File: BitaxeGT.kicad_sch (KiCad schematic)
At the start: 11 parts

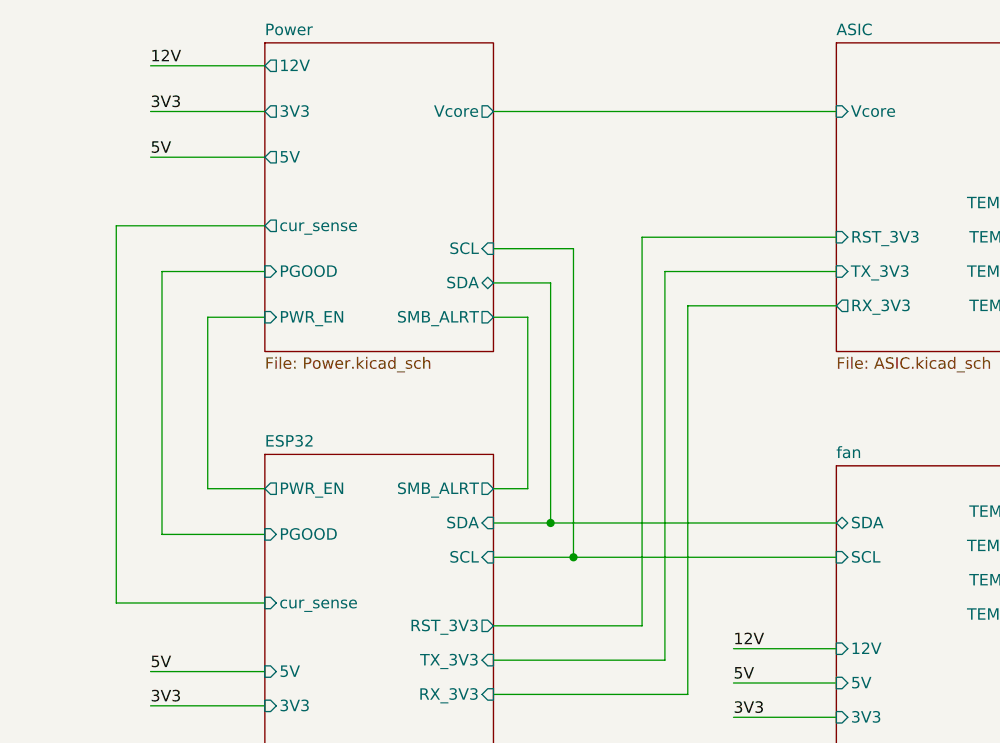
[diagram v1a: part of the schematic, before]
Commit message: fixed unused input on level shifter. Attached Vcore to ADC pin on the ESP32 for monitoring.
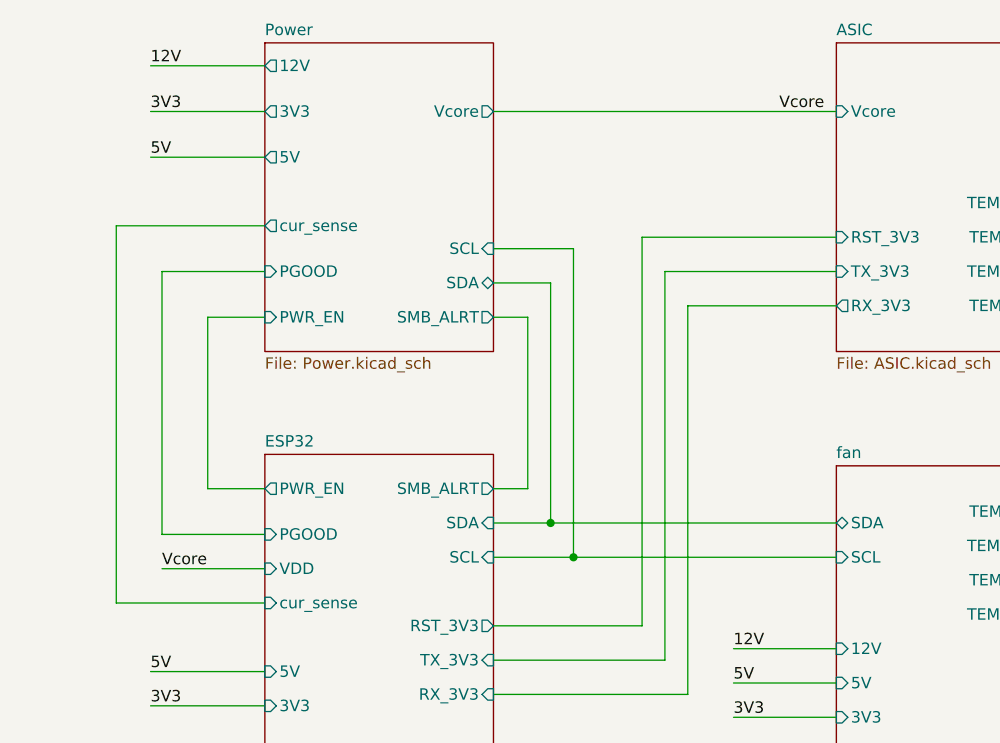
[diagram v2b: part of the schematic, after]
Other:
- sheet ESP32 ports: added VDD; removed none
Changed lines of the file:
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@@
+	(wire
+		(pts
+			(xy 105.41 101.6) (xy 116.84 101.6)
+		)
+		(stroke
+			(width 0)
+			(type default)
+		)
+	)
 	(wire
 		(pts
@@
 		)
 	)
-	(label "5V"
-		(at 104.14 55.88 0)
+	(label "Vcore"
+		(at 105.41 101.6 0)
 		(fields_autoplaced yes)
 		(effects
@@
 		)
 	)
-	(label "3V3"
-		(at 168.91 118.11 0)
+	(label "5V"
+		(at 104.14 55.88 0)
 		(fields_autoplaced yes)
 		(effects
@@
 		)
 	)
-	(label "5V"
-		(at 217.17 48.26 180)
+	(label "3V3"
+		(at 168.91 118.11 0)
 		(fields_autoplaced yes)
 		(effects
@@
 				(size 1.27 1.27)
 			)
-			(justify right bottom)
-		)
-	)
-	(label "3V3"
-		(at 217.17 52.07 180)
+			(justify left bottom)
+		)
+	)
+	(label "5V"
+		(at 217.17 48.26 180)
 		(fields_autoplaced yes)
 		(effects
@@
 		)
 	)
+	(label "3V3"
+		(at 217.17 52.07 180)
+		(fields_autoplaced yes)
+		(effects
+			(font
+				(size 1.27 1.27)
+			)
+			(justify right bottom)
+		)
+	)
 	(label "12V"
 		(at 104.14 45.72 0)
+		(fields_autoplaced yes)
+		(effects
+			(font
+				(size 1.27 1.27)
+			)
+			(justify left bottom)
+		)
+	)
+	(label "Vcore"
+		(at 173.99 50.8 0)
 		(fields_autoplaced yes)
 		(effects
@@
 			(effects
 				(font
+					(size 1.27 1.27)
+				)
+				(justify left)
+			)
+		)
+		(pin "VDD" input
+			(at 116.84 101.6 180)
+			(effects
+				(font

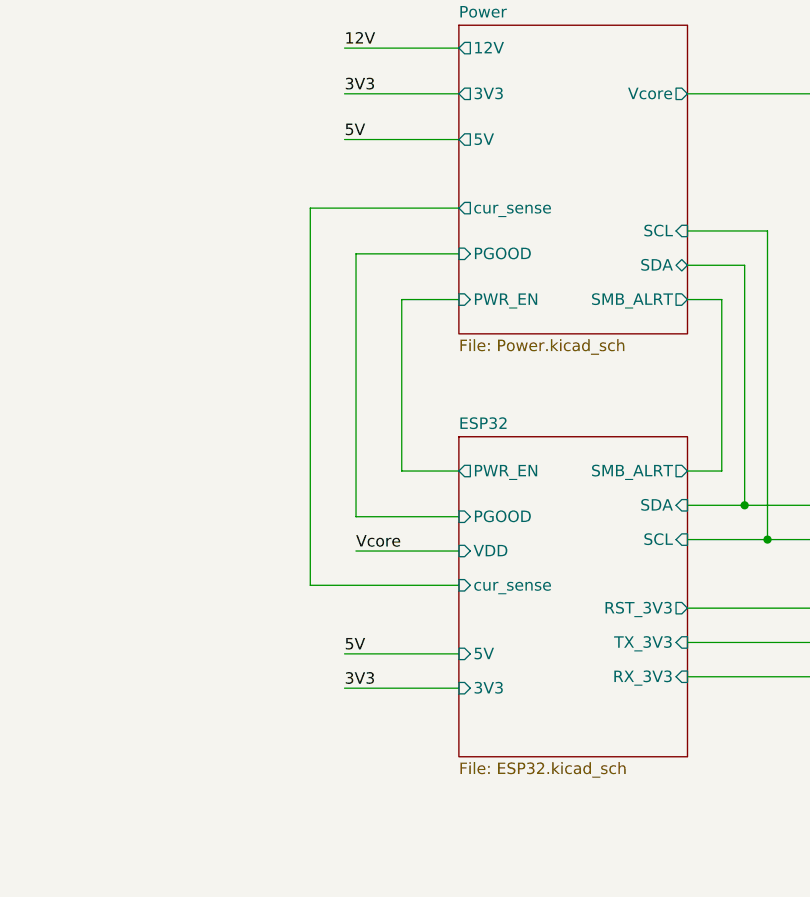
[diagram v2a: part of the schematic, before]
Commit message: added Vsupply to BAP. Cleaning up library paths. Moving 12V vias out of Bitaxe logo
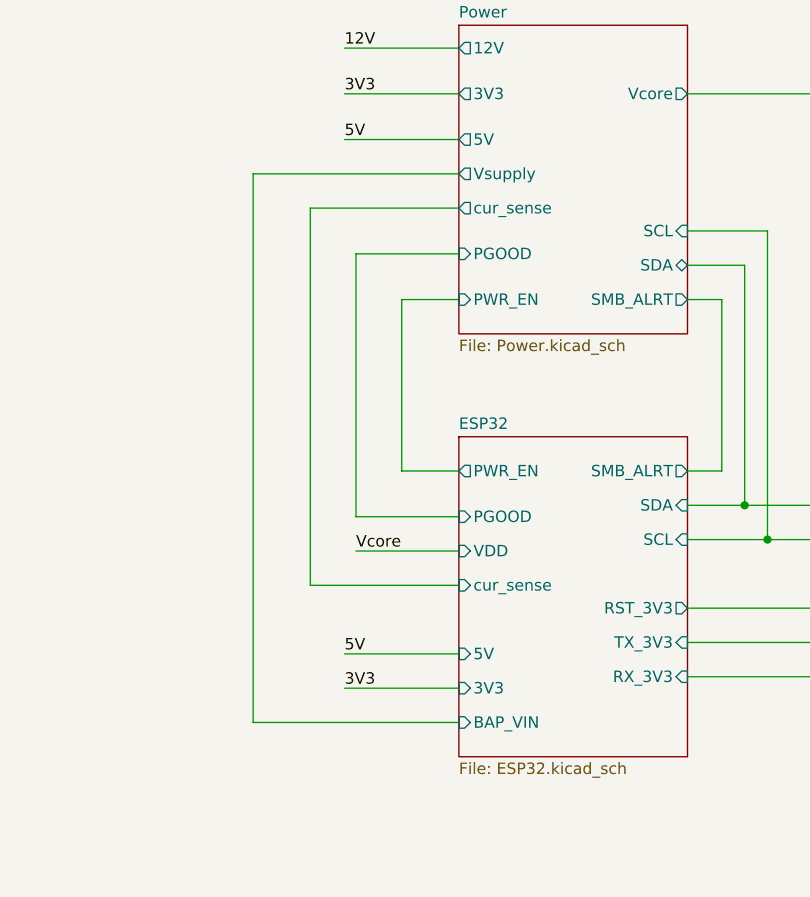
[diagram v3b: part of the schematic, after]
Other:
- sheet ESP32 ports: added BAP_VIN; removed none
- sheet Power ports: added Vsupply; removed none
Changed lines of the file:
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@@
+	(wire
+		(pts
+			(xy 116.84 59.69) (xy 93.98 59.69)
+		)
+		(stroke
+			(width 0)
+			(type default)
+		)
+	)
 	(wire
 		(pts
@@
 		(pts
 			(xy 104.14 113.03) (xy 116.84 113.03)
+		)
+		(stroke
+			(width 0)
+			(type default)
+		)
+	)
+	(wire
+		(pts
+			(xy 93.98 120.65) (xy 116.84 120.65)
+		)
+		(stroke
+			(width 0)
+			(type default)
+		)
+	)
+	(wire
+		(pts
+			(xy 93.98 59.69) (xy 93.98 120.65)
 		)
 		(stroke
@@
 			)
 		)
+		(pin "BAP_VIN" input
+			(at 116.84 120.65 180)
+			(effects
+				(font
+					(size 1.27 1.27)
+				)
+				(justify left)
+			)
+		)
 		(instances
 			(project "BitaxeGT"
@@
 			(effects
 				(font
+					(size 1.27 1.27)
+				)
+				(justify left)
+			)
+		)
+		(pin "Vsupply" output
+			(at 116.84 59.69 180)
+			(effects
+				(font

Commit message: BOM updates
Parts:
- HS1: now left out of the parts list
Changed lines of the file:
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@@
 		(unit 1)
 		(exclude_from_sim yes)
-		(in_bom yes)
+		(in_bom no)
 		(on_board yes)
 		(dnp no)

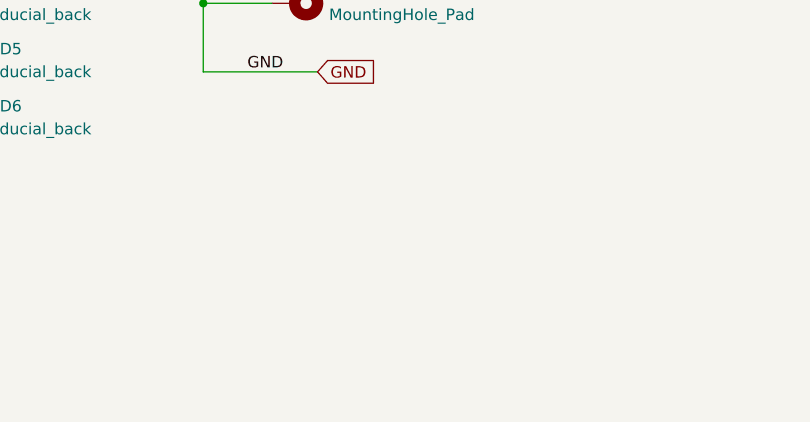
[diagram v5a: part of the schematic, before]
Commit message: mounting holes, removed smd fan header
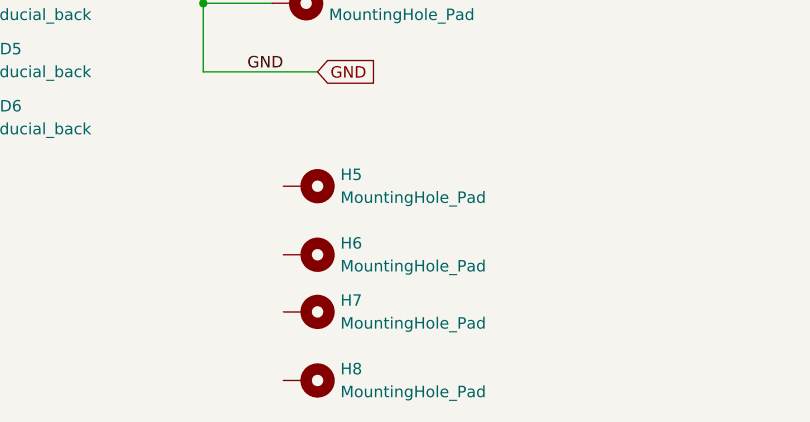
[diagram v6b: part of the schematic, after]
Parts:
- added H5, H6, H7, H8: MountingHole_Pad, bitaxe:Sinhoo SMTSO3015CTJ, symbol Mechanical:MountingHole_Pad

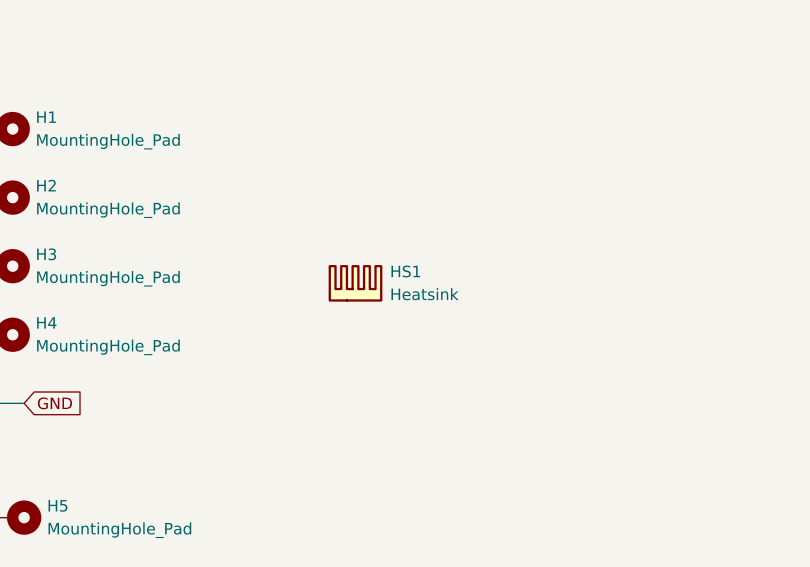
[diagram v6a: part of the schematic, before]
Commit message: fixed 12V / VIN net descrepancy
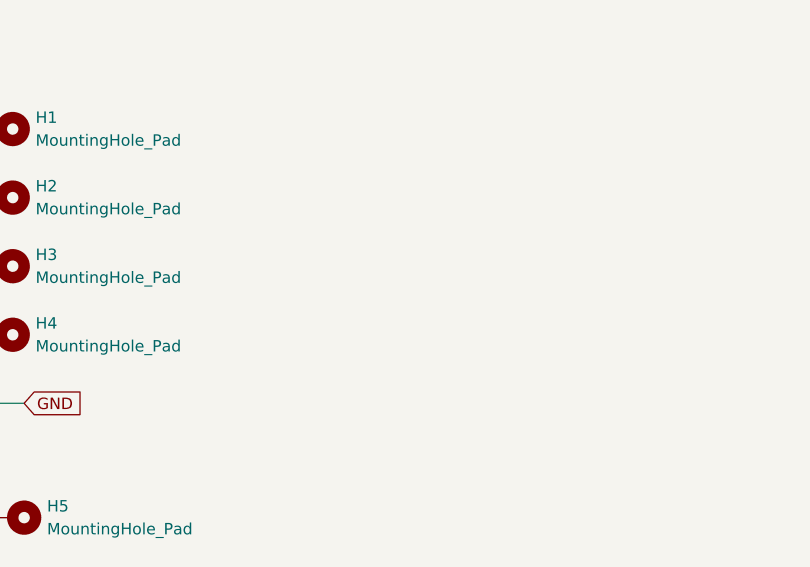
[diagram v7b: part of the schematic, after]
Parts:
- removed HS1: Heatsink, bitaxe:Heatsink-BitaxeGT, symbol Mechanical:Heatsink
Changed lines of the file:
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@@
 (kicad_sch
-	(version 20231120)
+	(version 20250114)
 	(generator "eeschema")
-	(generator_version "8.0")
+	(generator_version "9.0")
 	(paper "A3")
 	(title_block
@@
 	(label "3V3"
 		(at 104.14 116.84 0)
-		(fields_autoplaced yes)
 		(effects
 			(font
@@
 	(label "GND"
 		(at 80.01 182.88 180)
-		(fields_autoplaced yes)
 		(effects
 			(font
@@
 	(label "3V3"
 		(at 104.14 50.8 0)
-		(fields_autoplaced yes)
 		(effects
 			(font
@@
 	(label "Vcore"
 		(at 105.41 101.6 0)
-		(fields_autoplaced yes)
 		(effects
 			(font
@@
 	(label "5V"
 		(at 104.14 55.88 0)
-		(fields_autoplaced yes)
 		(effects
 			(font
@@
 	(label "3V3"
 		(at 168.91 118.11 0)
-		(fields_autoplaced yes)
 		(effects
 			(font
@@
 	(label "5V"
 		(at 217.17 48.26 180)
-		(fields_autoplaced yes)
 		(effects
 			(font
@@
 	(label "3V3"
 		(at 217.17 52.07 180)
-		(fields_autoplaced yes)
 		(effects
 			(font
@@
 	(label "12V"
 		(at 104.14 45.72 0)
-		(fields_autoplaced yes)
 		(effects
 			(font
@@
 	(label "Vcore"
 		(at 173.99 50.8 0)
-		(fields_autoplaced yes)
 		(effects
 			(font
@@
 	(label "5V"
 		(at 168.91 114.3 0)
-		(fields_autoplaced yes)
 		(effects
 			(font
@@
 	(label "12V"
 		(at 168.91 110.49 0)
-		(fields_autoplaced yes)
 		(effects
 			(font
@@
 	(label "5V"
 		(at 104.14 113.03 0)
-		(fields_autoplaced yes)
 		(effects
 			(font
@@
 	)
 	(symbol
-		(lib_id "Mechanical:Heatsink")
-		(at 120.65 171.45 0)
-		(unit 1)
-		(exclude_from_sim yes)
-		(in_bom no)
-		(on_board yes)
-		(dnp no)
-		(fields_autoplaced yes)
-		(property "Reference" "HS1"
-			(at 124.46 168.2749 0)
-			(effects
-				(font
-					(size 1.27 1.27)
-				)
-				(justify left)
-			)
-		)
-		(property "Value" "Heatsink"
-			(at 124.46 170.8149 0)
-			(effects
-				(font
-					(size 1.27 1.27)
-				)
-				(justify left)
-			)
-		)
-		(property "Footprint" "bitaxe:Heatsink-BitaxeGT"
-			(at 120.9548 171.45 0)
-			(effects
-				(font
-					(size 1.27 1.27)
-				)
-				(hide yes)
-			)
-		)
-		(property "Datasheet" "~"
-			(at 120.9548 171.45 0)
-			(effects
-				(font
-					(size 1.27 1.27)
-				)
-				(hide yes)
-			)
-		)
-		(property "Description" "Heatsink"
-			(at 120.65 171.45 0)
-			(effects
-				(font
-					(size 1.27 1.27)
-				)
-				(hide yes)
-			)
-		)
-		(property "partnum" ""
-			(at 120.65 171.45 0)
-			(effects
-				(font
-					(size 1.27 1.27)
-				)
-				(hide yes)
-			)
-		)
-		(instances
-			(project ""
-				(path "/61fe8d2c-9301-4ad9-8caf-c47acfa835b0"
-					(reference "HS1")
-					(unit 1)
-				)
-			)
-		)
-	)
-	(symbol
 		(lib_id "Mechanical:MountingHole_Pad")
 		(at 82.55 217.17 270)
@@
 		(at 116.84 88.9)
 		(size 25.4 35.56)
+		(exclude_from_sim no)
+		(in_bom yes)
+		(on_board yes)
+		(dnp no)
 		(fields_autoplaced yes)
 		(stroke
@@
 		(at 116.84 43.18)
 		(size 25.4 34.29)
+		(exclude_from_sim no)
+		(in_bom yes)
+		(on_board yes)
+		(dnp no)
 		(fields_autoplaced yes)
 		(stroke
@@
 		(at 180.34 43.18)
 		(size 24.13 34.29)
+		(exclude_from_sim no)
+		(in_bom yes)
+		(on_board yes)
+		(dnp no)
 		(fields_autoplaced yes)
 		(stroke
@@
 		(at 180.34 90.17)
 		(size 24.13 34.29)
+		(exclude_from_sim no)
+		(in_bom yes)
+		(on_board yes)
+		(dnp no)
 		(fields_autoplaced yes)
 		(stroke
@@
 		)
 	)
+	(embedded_fonts no)
 )

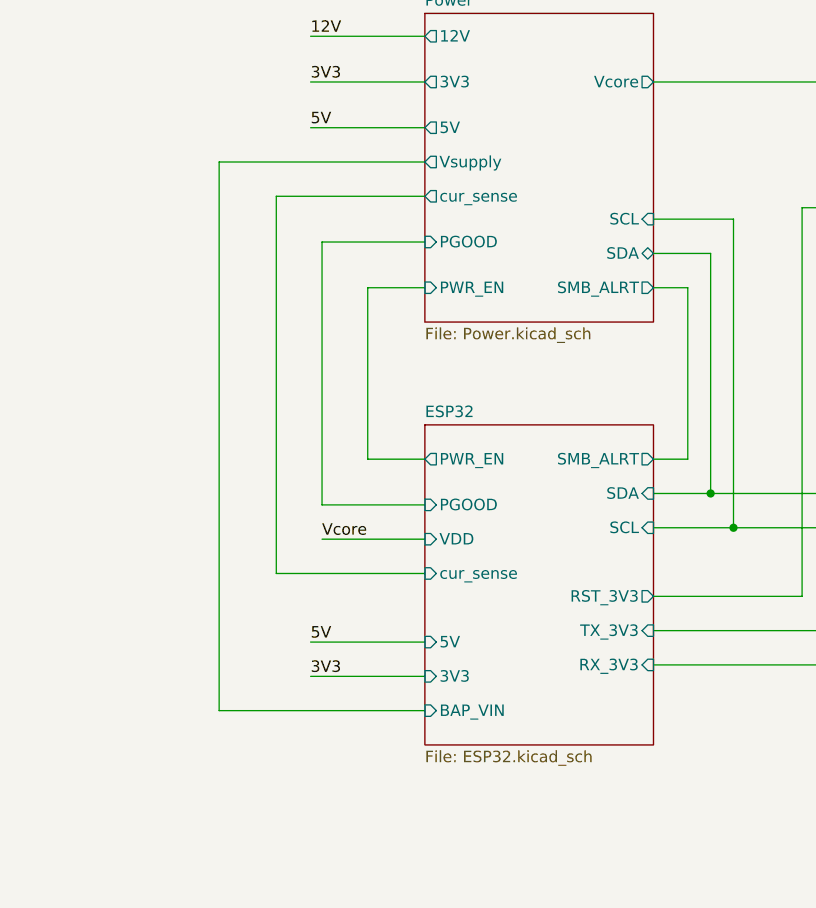
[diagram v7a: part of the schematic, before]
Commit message: fixed minor DRC stuff. re-attached BAP VIN. bumped version to 800xx. deleted old gerbers
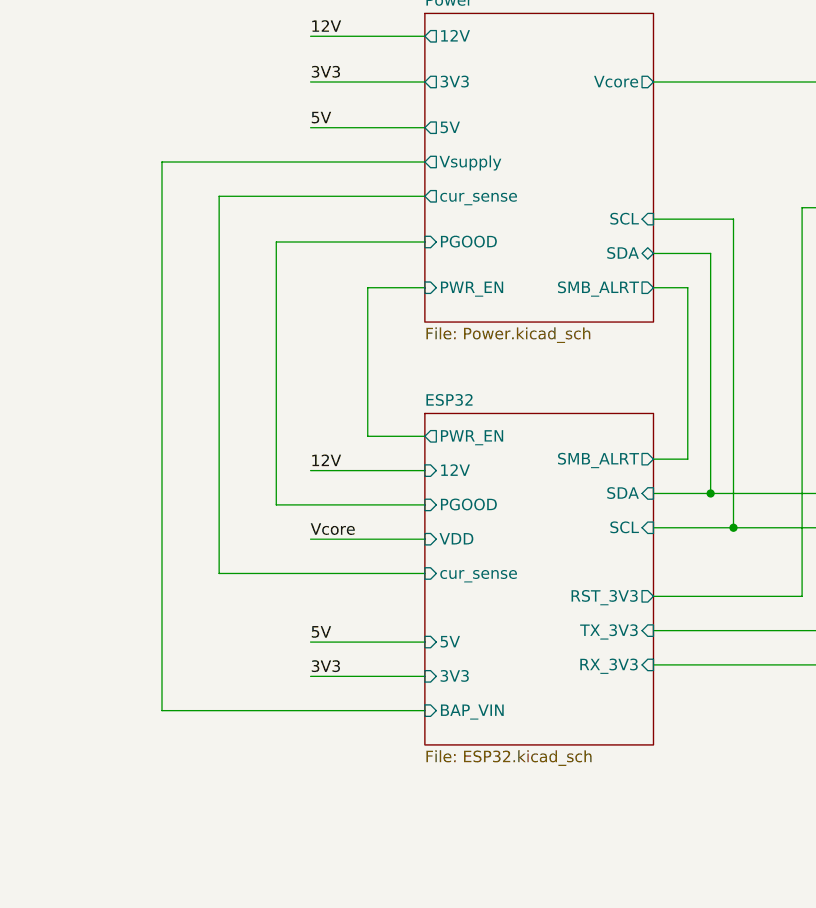
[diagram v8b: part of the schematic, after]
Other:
- sheet ESP32 ports: added 12V; removed none
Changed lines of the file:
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@@
 	(title_block
 		(title "Bitaxe Gamma Turbo")
-		(date "2024-10-15")
-		(rev "800")
+		(date "2025-02-28")
+		(rev "800xx")
 	)
 	(junction
@@
 	(wire
 		(pts
-			(xy 100.33 63.5) (xy 100.33 105.41)
+			(xy 93.98 63.5) (xy 93.98 105.41)
 		)
 		(stroke
@@
 	(wire
 		(pts
-			(xy 100.33 105.41) (xy 116.84 105.41)
+			(xy 93.98 105.41) (xy 116.84 105.41)
 		)
 		(stroke
@@
 	(wire
 		(pts
-			(xy 105.41 68.58) (xy 105.41 97.79)
+			(xy 100.33 68.58) (xy 100.33 97.79)
 		)
 		(stroke
@@
 	(wire
 		(pts
-			(xy 110.49 92.71) (xy 116.84 92.71)
-		)
-		(stroke
-			(width 0)
-			(type default)
-		)
-	)
-	(wire
-		(pts
-			(xy 116.84 59.69) (xy 93.98 59.69)
+			(xy 110.49 90.17) (xy 116.84 90.17)
+		)
+		(stroke
+			(width 0)
+			(type default)
+		)
+	)
+	(wire
+		(pts
+			(xy 116.84 59.69) (xy 87.63 59.69)
 		)
 		(stroke
@@
 	(wire
 		(pts
-			(xy 116.84 63.5) (xy 100.33 63.5)
-		)
-		(stroke
-			(width 0)
-			(type default)
-		)
-	)
-	(wire
-		(pts
-			(xy 105.41 101.6) (xy 116.84 101.6)
+			(xy 116.84 63.5) (xy 93.98 63.5)
+		)
+		(stroke
+			(width 0)
+			(type default)
+		)
+	)
+	(wire
+		(pts
+			(xy 104.14 101.6) (xy 116.84 101.6)
 		)
 		(stroke
@@
 	(wire
 		(pts
-			(xy 110.49 73.66) (xy 110.49 92.71)
+			(xy 110.49 73.66) (xy 110.49 90.17)
 		)
 		(stroke
@@
 	(wire
 		(pts
-			(xy 93.98 120.65) (xy 116.84 120.65)
-		)
-		(stroke
-			(width 0)
-			(type default)
-		)
-	)
-	(wire
-		(pts
-			(xy 93.98 59.69) (xy 93.98 120.65)
+			(xy 87.63 120.65) (xy 116.84 120.65)
+		)
+		(stroke
+			(width 0)
+			(type default)
+		)
+	)
+	(wire
+		(pts
+			(xy 87.63 59.69) (xy 87.63 120.65)
 		)
 		(stroke
@@
 	(wire
 		(pts
-			(xy 105.41 97.79) (xy 116.84 97.79)
+			(xy 104.14 93.98) (xy 116.84 93.98)
+		)
+		(stroke
+			(width 0)
+			(type default)
+		)
+	)
+	(wire
+		(pts
+			(xy 100.33 97.79) (xy 116.84 97.79)
 		)
 		(stroke
@@
 	(wire
 		(pts
-			(xy 105.41 68.58) (xy 116.84 68.58)
+			(xy 100.33 68.58) (xy 116.84 68.58)
 		)
 		(stroke
@@
 	)
 	(label "Vcore"
-		(at 105.41 101.6 0)
+		(at 104.14 101.6 0)
 		(effects
 			(font
@@
 	(label "12V"
 		(at 168.91 110.49 0)
+		(effects
+			(font
+				(size 1.27 1.27)
+			)
+			(justify left bottom)
+		)
+	)
+	(label "12V"
+		(at 104.14 93.98 0)
 		(effects
 			(font
@@
 	)
 	(sheet
-		(at 116.84 88.9)
-		(size 25.4 35.56)
+		(at 116.84 87.63)
+		(size 25.4 36.83)
 		(exclude_from_sim no)
 		(in_bom yes)
@@
 		)
 		(property "Sheetname" "ESP32"
-			(at 116.84 88.1884 0)
+			(at 116.84 86.9184 0)
 			(effects
 				(font
@@
 		)
 		(pin "PWR_EN" output
-			(at 116.84 92.71 180)
+			(at 116.84 90.17 180)
 			(effects
 				(font
@@
 			(effects
 				(font
+					(size 1.27 1.27)
+				)
+				(justify left)
+			)
+		)
+		(pin "12V" input
+			(at 116.84 93.98 180)
+			(effects
+				(font
